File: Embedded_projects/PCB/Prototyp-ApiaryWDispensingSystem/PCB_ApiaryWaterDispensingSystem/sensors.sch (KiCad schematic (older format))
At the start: 11 parts

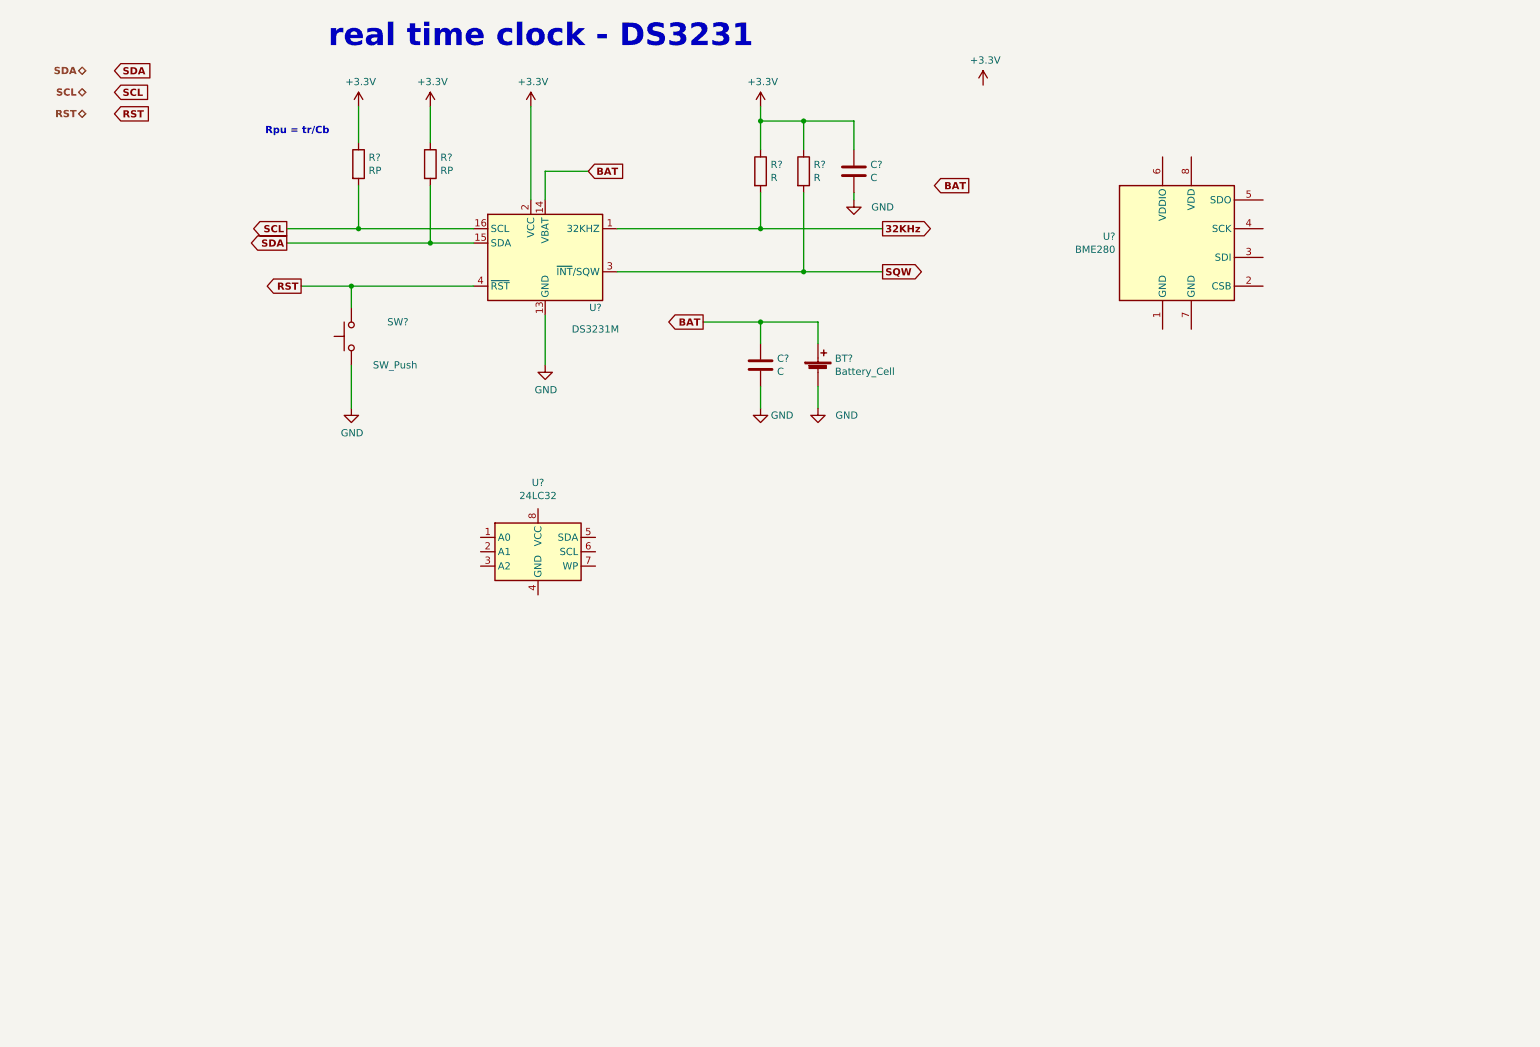
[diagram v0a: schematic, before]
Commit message: added x-tal and his footprints for microcontroller schematics, user button
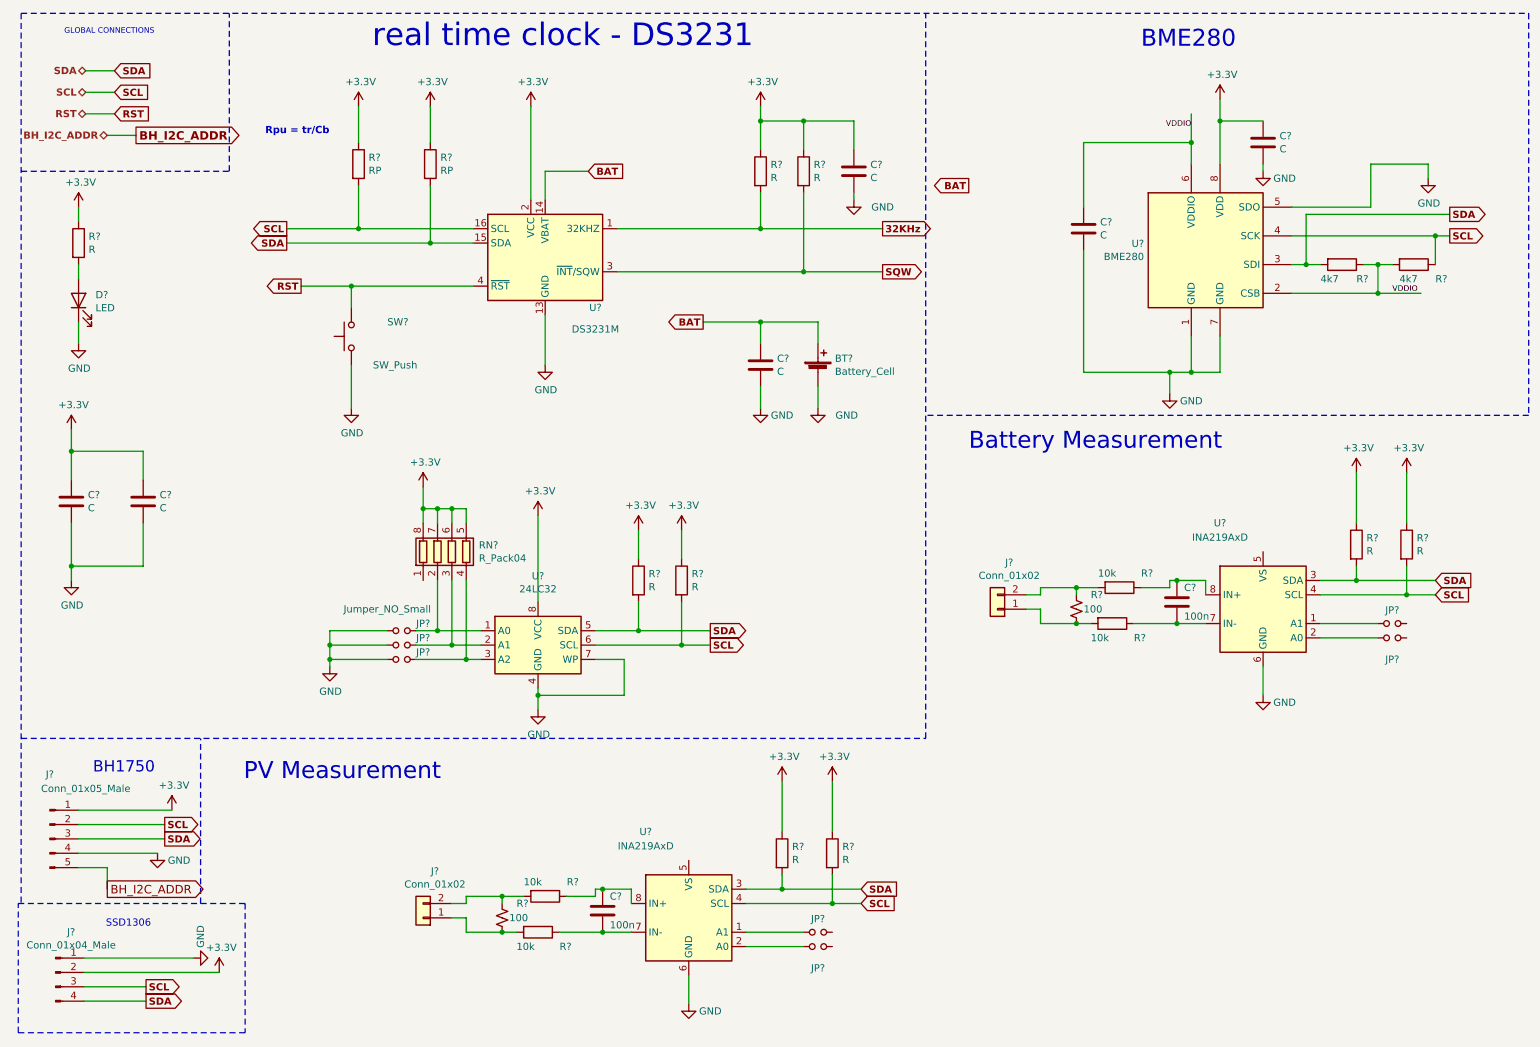
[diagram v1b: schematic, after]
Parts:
- added C? (x4): C, symbol Device:C
- added C? (x2): 100n, symbol Device:C
- added D?: LED, symbol Device:LED
- added J?: Conn_01x05_Male, symbol Connector:Conn_01x05_Male
- added J?: Conn_01x04_Male, symbol Connector:Conn_01x04_Male
- added J? (x2): Conn_01x02, symbol Connector_Generic:Conn_01x02
- added JP? (x7): Jumper_NO_Small, symbol Device:Jumper_NO_Small
- added R? (x7): R, symbol Device:R
- added R? (x2): 4k7, symbol Device:R
- added R? (x2): 100, symbol Device:R_Small_US
- added R? (x4): 10k, symbol Device:R
- added RN?: R_Pack04, symbol Device:R_Pack04
- added U? (x2): INA219AxD, Package_SO:SOIC-8_3.9x4.9mm_P1.27mm, symbol Analog_ADC:INA219AxD
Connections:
- net +3V3: now also U?.8 (VCC), U?.8 (VDD), C?.1, C?.1, C?.1, J?.1 (Pin_1), J?.2 (Pin_2), R?.1, R?.1, R?.1, R?.1, R?.1, R?.1, R?.1, RN?.5 (R4.2), RN?.6 (R3.2), RN?.7 (R2.2), RN?.8 (R1.2)
- net GND: now also U?.1 (GND), U?.4 (GND), U?.5 (SDO), U?.7 (GND), U?.7 (WP), C?.2, C?.2, C?.2, C?.2, D?.1 (K), J?.1 (Pin_1), J?.4 (Pin_4), JP?.1, JP?.1, JP?.1, U?.6 (GND), U?.6 (GND)
- net SCL: now also U?.4 (SCK), U?.6 (SCL), J?.2 (Pin_2), J?.3 (Pin_3), R?.1, R?.2, R?.2, R?.2, U?.4 (SCL), U?.4 (SCL)
- net SDA: now also U?.3 (SDI), U?.5 (SDA), J?.3 (Pin_3), J?.4 (Pin_4), R?.2, R?.2, R?.2, R?.2, U?.3 (SDA), U?.3 (SDA)
- net VDDIO: now reaches U?.2 (CSB)
- net VDDIO: now also U?.6 (VDDIO), C?.1, R?.1, R?.2
- net at U?.1 (A0): now also JP?.2, RN?.2 (R2.1)
- net at U?.2 (A1): now also JP?.2, RN?.3 (R3.1)
- net at U?.3 (A2): now also JP?.2, RN?.4 (R4.1)
- new net: D?.2 (A), R?.2
- new net: JP?.1, U?.1 (A1) (x2)
- new net: JP?.1, U?.2 (A0) (x2)
- new net: C?.2, R?.1, U?.7 (IN-) (x2)
- new net: C?.1, R?.1, U?.8 (IN+) (x2)
- new net: J?.2 (Pin_2), R?.1, R?.2 (x2)
- new net: J?.1 (Pin_1), R?.2, R?.2 (x2)
- new net BH_I2C_ADDR: J?.5 (Pin_5)
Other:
- note added: "BH1750"
- note added: "BME280"
- note added: "Battery Measurement"
- note added: "GLOBAL CONNECTIONS"
- note added: "PV Measurement"
- note added: "SSD1306"
- moved on the sheet: U?

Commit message: added lot of changes to project #3
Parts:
- removed C? (x2): 100n, symbol Device:C
- removed R? (x4): 10k, symbol Device:R
- added C? (x3): 100n, Capacitor_SMD:C_0805_2012Metric, symbol Device:C
- added I2C: Conn_01x02, symbol Connector_Generic:Conn_01x02
- added R? (x4): R, Resistor_SMD:R_0805_2012Metric, symbol Device:R
- C? (x5): value C -> 100n; footprint (none) -> Capacitor_SMD:C_0805_2012Metric
- C?: value C -> 100n
- D?: footprint (none) -> Diode_SMD:D_0805_2012Metric
- R? (x7): footprint (none) -> Resistor_SMD:R_0805_2012Metric
- R? (x4): value R -> 4k7; footprint (none) -> Resistor_SMD:R_0805_2012Metric
- R? (x2): value R -> 4k7
- R? (x2): footprint (none) -> Resistor_SMD:R_2512_6332Metric
- SW?: footprint (none) -> Button_Switch_SMD:SW_Push_1P1T_NO_6x6mm_H9.5mm
- gave numbers to parts that had none: 2
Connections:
- net BH_I2C_ADDR is gone; now on net GND: J?.5 (Pin_5)
- net +3V3: now also A1.2, A2.2, JP?.2, JP?.2, U?.5 (VS), U?.5 (VS), C?.1, C?.1, C?.1
- net GND: now also C?.2, C?.2, C?.2, R?.2, R?.2, R?.2, R?.2
- net SCL: now also I2C.2 (Pin_2)
- net SDA: now also I2C.1 (Pin_1)
- net at JP?.1, U?.1 (A1): now also R?.1
- net at JP?.1, U?.2 (A0): now also R?.1
- net at U?.7 (IN-): now also J?.1 (Pin_1), R?.2 (x2)
- net at U?.8 (IN+): now also J?.2 (Pin_2), R?.1 (x2)
- net at A1.1, U?.1 (A1): now also R?.1
- net at A2.1, U?.2 (A0): now also R?.1
- no-connect marks 0 -> 2
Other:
- note added: "Wyświetlacz możliwy do zmiany \nprzy zastosowaniu touchgfx"

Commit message: Many design changes have been added over the past few months #3
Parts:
- removed R?: R, Resistor_SMD:R_0805_2012Metric, symbol Device:R
- added J?: Conn_01x03, symbol Connector_Generic:Conn_01x03
- A1, A2: renamed from JP?; footprint (none) -> Jumper:SolderJumper-2_P1.3mm_Open_TrianglePad1.0x1.5mm
- C? (x6): footprint Capacitor_SMD:C_0805_2012Metric -> Capacitor_SMD:C_0603_1608Metric
- C?: footprint (none) -> Capacitor_SMD:C_0603_1608Metric
- I2C: footprint (none) -> Connector_PinSocket_2.54mm:PinSocket_1x02_P2.54mm_Vertical
- J?: footprint (none) -> Connector_PinSocket_2.54mm:PinSocket_1x05_P2.54mm_Vertical
- J?: footprint (none) -> Connector_PinSocket_2.54mm:PinSocket_1x04_P2.54mm_Vertical
- J? (x2): footprint (none) -> TerminalBlock_4Ucon:TerminalBlock_4Ucon_1x02_P3.50mm_Horizontal
- R? (x10): footprint Resistor_SMD:R_0805_2012Metric -> Resistor_SMD:R_0603_1608Metric
- R? (x2): footprint (none) -> Resistor_SMD:R_0603_1608Metric
- RN?: footprint (none) -> Resistor_SMD:R_Array_Convex_4x0603
- renumbered A1 to A3
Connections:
- net GND: now also J?.1 (Pin_1)
- net +3V3 renamed VDD
- net VDD: now also J?.2 (Pin_2)
- net 32KHz: no longer names the net of U?.1 (32KHZ)
- net RST: no longer names the net of SW?.2, U?.4 (~RST)
- new net ADC1_IN0: J?.3 (Pin_3)
- no-connect marks 2 -> 3
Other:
- note added: "good"

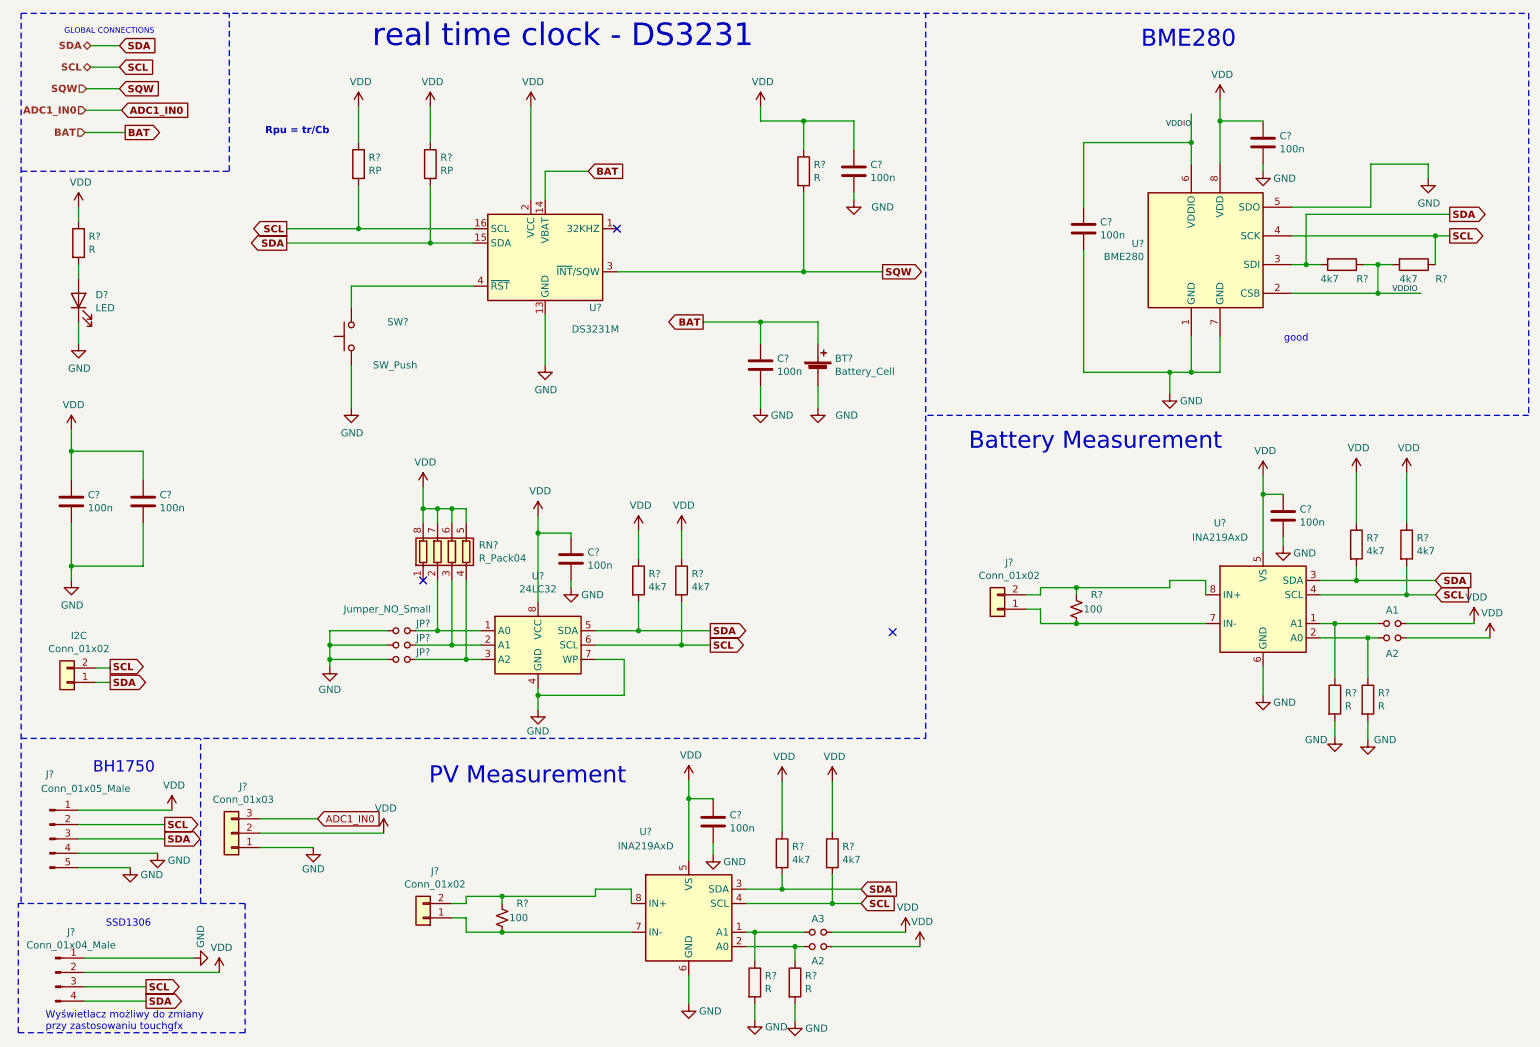
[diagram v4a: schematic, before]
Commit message: All signal has been routed, the analog part needs to be completed
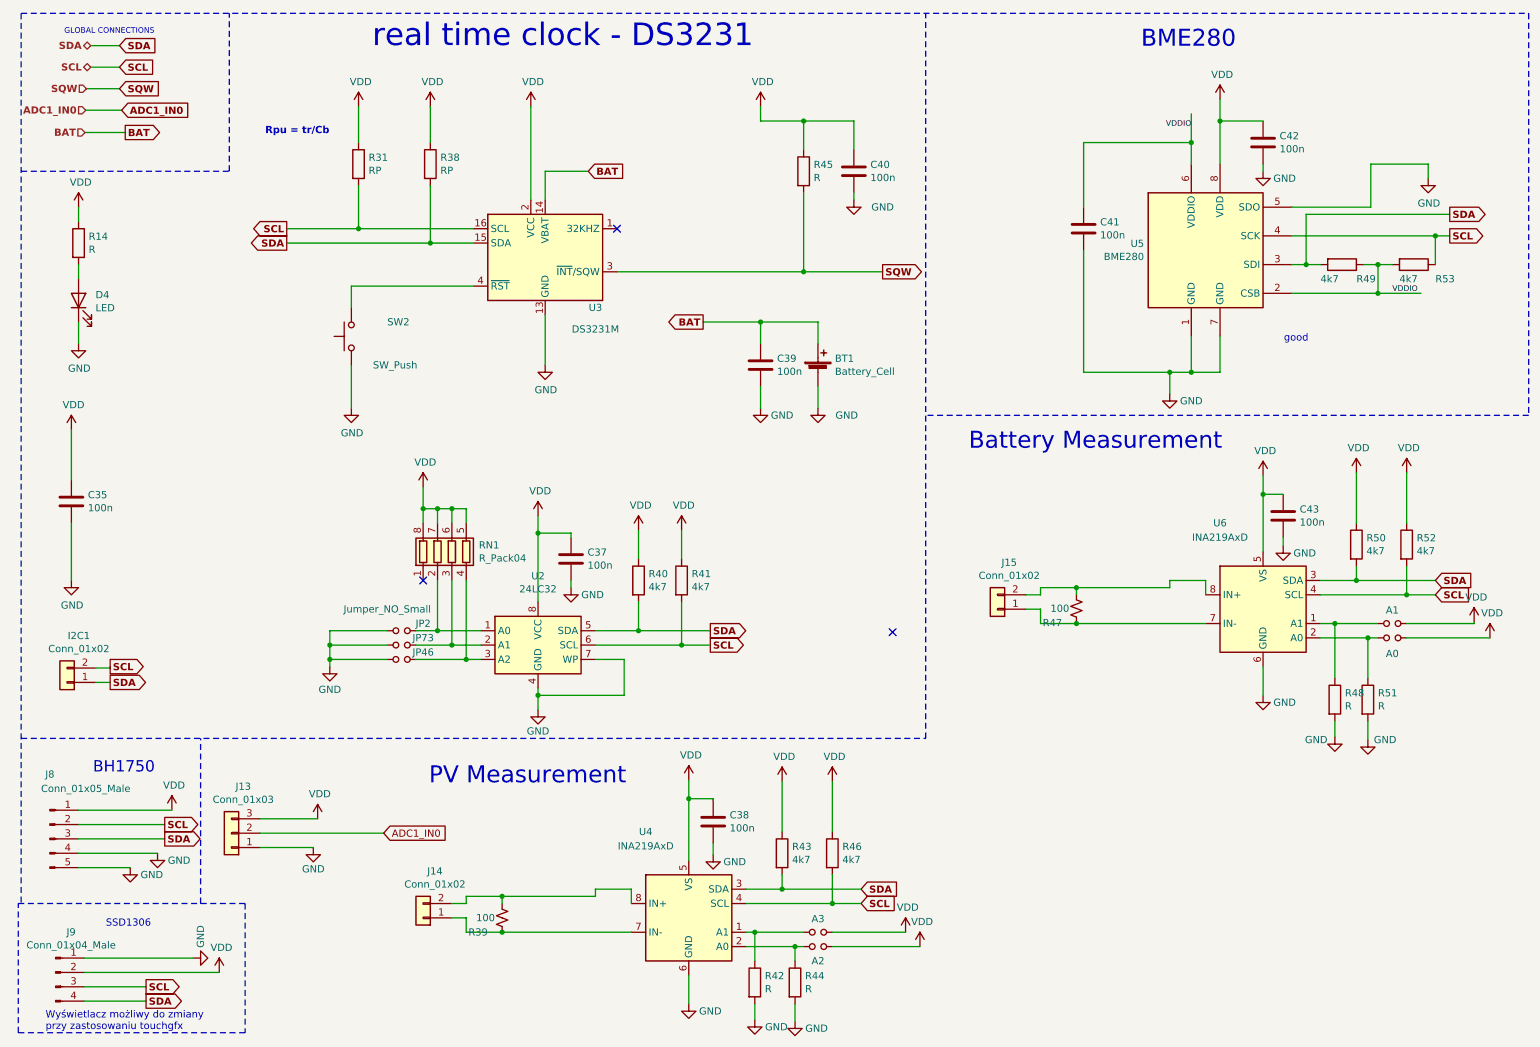
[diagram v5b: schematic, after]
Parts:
- removed C?: 100n, Capacitor_SMD:C_0603_1608Metric, symbol Device:C
- A2, A3: footprint (none) -> Jumper:SolderJumper-2_P1.3mm_Open_TrianglePad1.0x1.5mm
- C38, C43: renamed from C?; footprint Capacitor_SMD:C_0805_2012Metric -> Capacitor_SMD:C_0603_1608Metric
- J13: renamed from J?; footprint (none) -> TerminalBlock_TE-Connectivity:TerminalBlock_TE_282834-3_1x03_P2.54mm_Horizontal
- J8: renamed from J?; footprint Connector_PinSocket_2.54mm:PinSocket_1x05_P2.54mm_Vertical -> Connector_PinSocket_1.27mm:PinSocket_1x05_P1.27mm_Vertical
- JP2, JP46, JP73: renamed from JP?; footprint (none) -> Jumper:SolderJumper-2_P1.3mm_Open_TrianglePad1.0x1.5mm
- R42, R43, R44, R46: renamed from R?; footprint Resistor_SMD:R_0805_2012Metric -> Resistor_SMD:R_0603_1608Metric
- U2: renamed from U?; footprint (none) -> ApiaryWaterDispensingSystem:24LC32
- gave numbers to parts that had none: 31
- renumbered A2 to A0, I2C to I2C1
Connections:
- net ADC1_IN0: now also J13.2 (Pin_2); no longer J13.3 (Pin_3)
- net VDD: now also J13.3 (Pin_3); no longer J13.2 (Pin_2)
- net at J15.1 (Pin_1), U6.7 (IN-): now also R47.1; no longer R47.2
- net at J15.2 (Pin_2), U6.8 (IN+): now also R47.2; no longer R47.1
- net at J14.1 (Pin_1), U4.7 (IN-): now also R39.1; no longer R39.2
- net at J14.2 (Pin_2), U4.8 (IN+): now also R39.2; no longer R39.1
